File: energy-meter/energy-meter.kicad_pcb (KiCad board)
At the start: 2 copper layers, 82 x 62.5 mm, 87 parts, among them J1 Screw_Terminal_01x04, J27 Conn_01x04_Male, K1 G5RL-U1A-E, P1 PineNut, Q10 AP3400, Q11 AP3400, Q12 AP3400, Q14 AP3400, T1 AP-2500, T2 BV 202 0154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

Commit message: continue changing schematic
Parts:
- removed C69, C74: 47p, Capacitor_SMD:C_0603_1608Metric_Pad1.05x0.95mm_HandSolder
- removed C71, C73, C75, C76: 270p, Capacitor_SMD:C_0603_1608Metric_Pad1.05x0.95mm_HandSolder
- removed J27: Conn_01x04_Male, Connector_PinHeader_2.54mm:PinHeader_1x04_P2.54mm_Vertical
- removed R56, R57, R58, R60, R61, R62: 1k, Resistor_SMD:R_0603_1608Metric_Pad1.05x0.95mm_HandSolder
- removed R59, R63: 4k7, Resistor_SMD:R_0603_1608Metric_Pad1.05x0.95mm_HandSolder
- removed R65, R77, R83: 390k, Resistor_SMD:R_0603_1608Metric_Pad1.05x0.95mm_HandSolder
- removed R76, R78: 10R, 200 mW, Resistor_SMD:R_1206_3216Metric_Pad1.42x1.75mm_HandSolder
- added R1: 50R, 0.1%, Resistor_SMD:R_0603_1608Metric_Pad1.05x0.95mm_HandSolder, F.Cu at (127.9, 77.5)
- added R2: 50R, 0.1%, Resistor_SMD:R_0603_1608Metric_Pad1.05x0.95mm_HandSolder, F.Cu at (127.9, 80.0)
- added R3: 50R, 0.1%, Resistor_SMD:R_0603_1608Metric_Pad1.05x0.95mm_HandSolder, F.Cu at (132.2, 77.5)
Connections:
- net /Modified LCR Meter/IN0 renamed /Modified LCR Meter/VOLTAGE0
- net /Modified LCR Meter/IN1 renamed /Modified LCR Meter/VOLTAGE1
- net /Modified LCR Meter/OUT0_OFFSET renamed Net-(U10-Pad12)
- net /Modified LCR Meter/OUT1_OFFSET renamed Net-(U10-Pad15)
- net Net-(J1-Pad1) renamed PE
- D12 pad 1: /Modified LCR Meter/OUT0B -> /Modified LCR Meter/CURRENT1
- D12 pad 13: /Modified LCR Meter/OUT0B -> /Modified LCR Meter/CURRENT1
- D12 pad 14: /Modified LCR Meter/OUT0B -> /Modified LCR Meter/CURRENT1
- D12 pad 2: /Modified LCR Meter/OUT0B -> /Modified LCR Meter/CURRENT1
- D12 pad 6: /Modified LCR Meter/OUT1 -> /Modified LCR Meter/CURRENT0
- D12 pad 7: /Modified LCR Meter/OUT1 -> /Modified LCR Meter/CURRENT0
- D12 pad 8: /Modified LCR Meter/OUT1 -> /Modified LCR Meter/CURRENT0
- D12 pad 9: /Modified LCR Meter/OUT1 -> /Modified LCR Meter/CURRENT0
- J1 pad 2: Net-(J1-Pad2) -> N
- J1 pad 3: Net-(J1-Pad3) -> L_IN
- J1 pad 4: Net-(J1-Pad4) -> L_OUT
- K1 pad 3: Net-(K1-Pad3) -> L_OUT
- K1 pad 4: Net-(K1-Pad4) -> L_IN
- K1 pad 5: Net-(K1-Pad5) -> L_IN
- K1 pad 6: Net-(K1-Pad6) -> L_OUT
- R64 pad 2: /Modified LCR Meter/OUT0 -> /Modified LCR Meter/CURRENT0
- R66 pad 2: /Modified LCR Meter/CURR0 -> /Modified LCR Meter/CURRENT0
- R67 pad 2: /Modified LCR Meter/CURR1 -> /Modified LCR Meter/CURRENT1
- R84 pad 3: /Modified LCR Meter/CURR0 -> /Modified LCR Meter/CURRENT0
- R84 pad 4: /Modified LCR Meter/OUT0 -> /Modified LCR Meter/CURRENT0
- R85 pad 1: /Modified LCR Meter/OUT0 -> /Modified LCR Meter/CURRENT0
- R85 pad 2: /Modified LCR Meter/CURR0 -> /Modified LCR Meter/CURRENT0
- R86 pad 1: /Modified LCR Meter/OUT0 -> /Modified LCR Meter/CURRENT0
- R86 pad 2: /Modified LCR Meter/CURR0 -> /Modified LCR Meter/CURRENT0
- R95 pad 1: /Modified LCR Meter/OUT0 -> /Modified LCR Meter/CURRENT0
- R95 pad 2: /Modified LCR Meter/CURR0 -> /Modified LCR Meter/CURRENT0
- T2 pad 1: Net-(T2-Pad1) -> L_IN
- T2 pad 4: (no net) -> N
- U10 pad 18: /Modified LCR Meter/CURR1 -> /Modified LCR Meter/CURRENT1
- U11 pad 18: /Modified LCR Meter/CURR1 -> /Modified LCR Meter/CURRENT1
- U12 pad 18: /Modified LCR Meter/CURR1 -> /Modified LCR Meter/CURRENT1
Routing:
- net /Modified LCR Meter/CURRENT1: track 0.00 -> 39.5 mm, vias 0 -> 3
- net /Modified LCR Meter/CURR1: track 39.5 -> 0.00 mm, vias 3 -> 0
- net /Modified LCR Meter/CURRENT0: track 0.00 -> 32.4 mm
- net /Modified LCR Meter/CURR0: track 32.4 -> 0.00 mm
- net (no net): track 0.00 -> 27.8 mm, vias 0 -> 4
- net /LCR Meter/U10B-: track 25.9 -> 0.00 mm, vias 4 -> 0
- net GND: track 188.9 -> 164.5 mm, vias 18 -> 15
- net Net-(C73-Pad2): track 13.4 -> 0.00 mm, vias 2 -> 0
- net /LCR Meter/DAC0: track 11.2 -> 0.00 mm
- net /DAC0: track 0.00 -> 11.2 mm
- net Net-(C76-Pad2): track 10.7 -> 0.00 mm
- net Net-(C71-Pad1): track 10.2 -> 0.00 mm
- net Net-(C69-Pad1): track 6.86 -> 0.00 mm
- net Net-(C74-Pad1): track 5.68 -> 0.00 mm, vias 2 -> 0
- net Net-(R59-Pad2): track 5.43 -> 0.00 mm
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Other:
- board text added: "Energy Meter v1 c3pb, snowball"
- board text removed: "0"
- board text removed: "0b"
- board text removed: "1"
- board text removed: "1b"
- board text removed: "LCR Meter v1 c3pb, snowball"

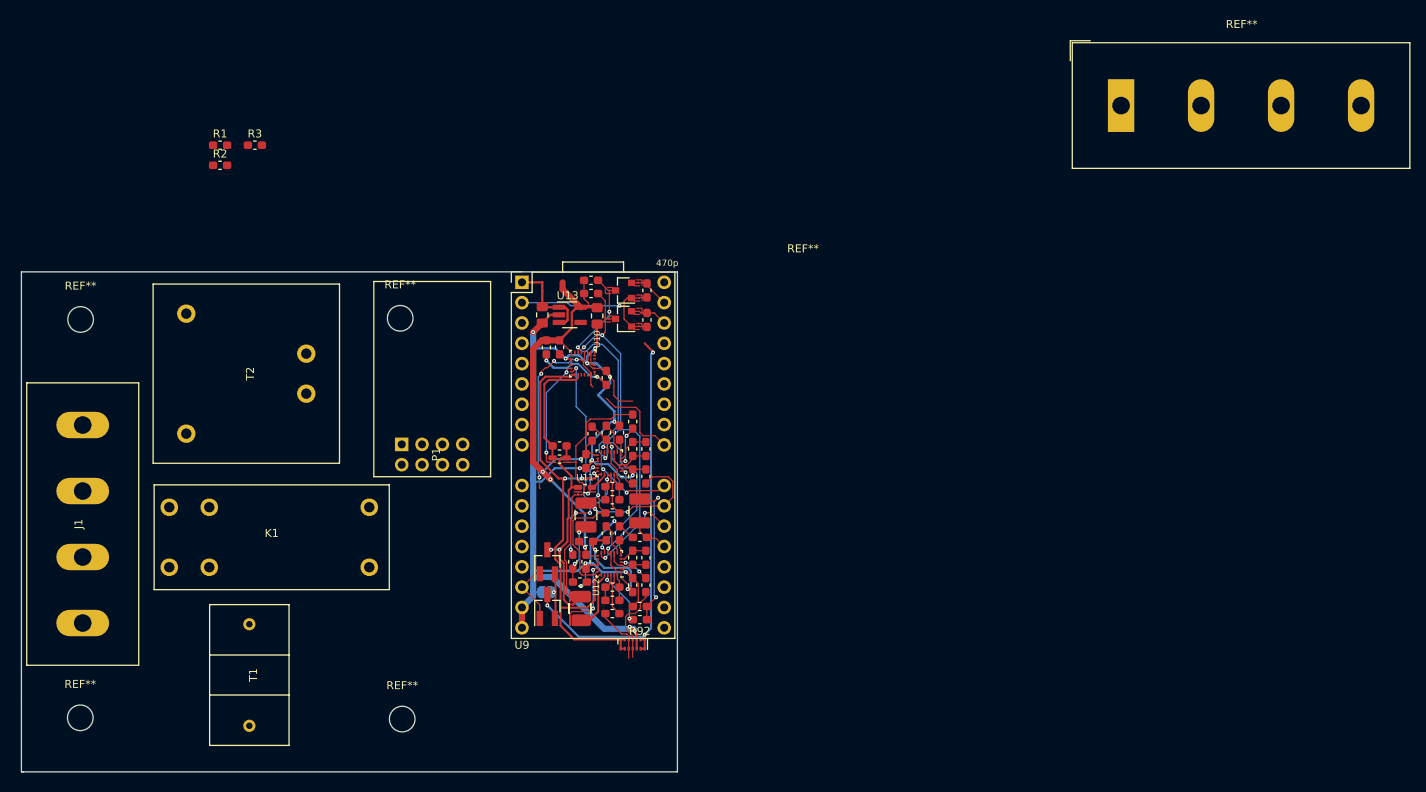
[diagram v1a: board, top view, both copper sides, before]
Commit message: remove two of the opamps
We can measure the voltage without an amplifier so let's do it. The other
was used for the LCR outputs, which we don't have here.
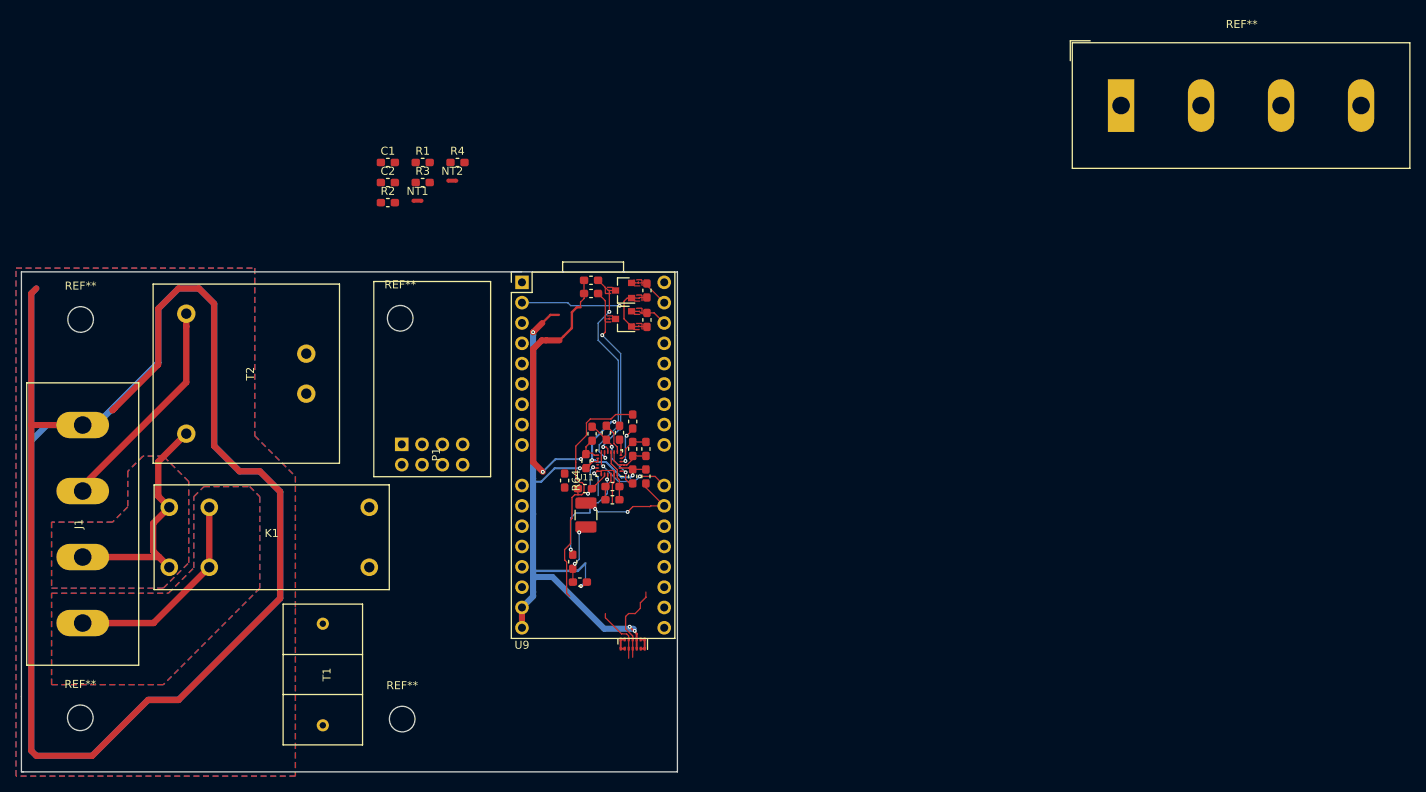
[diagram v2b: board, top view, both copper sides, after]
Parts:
- removed C65, C67, C70, C72: 100n, Capacitor_SMD:C_0603_1608Metric_Pad1.05x0.95mm_HandSolder
- removed C79, C80: 4.7p, Capacitor_SMD:C_0603_1608Metric_Pad1.05x0.95mm_HandSolder
- removed C81, C82: 1u, Capacitor_SMD:C_0805_2012Metric_Pad1.15x1.40mm_HandSolder
- removed C85: 270p, 1%, Capacitor_SMD:C_0603_1608Metric_Pad1.05x0.95mm_HandSolder
- removed FB1, FB3: 600R, 0.5A, Inductor_SMD:L_0603_1608Metric_Pad1.05x0.95mm_HandSolder
- removed JP20: SolderJumper_2_Open, Jumper:SolderJumper-2_P1.3mm_Open_RoundedPad1.0x1.5mm
- removed L5: 470u, Inductor_SMD:L_1210_3225Metric_Pad1.42x2.65mm_HandSolder
- removed Q12, Q14: AP3400, Package_TO_SOT_SMD:SOT-23_Handsoldering
- removed R67, R68, R69: 1k, Resistor_SMD:R_0603_1608Metric_Pad1.05x0.95mm_HandSolder
- removed R70, R71: 10k, Resistor_SMD:R_0603_1608Metric_Pad1.05x0.95mm_HandSolder
- removed R79, R80: 47k, Resistor_SMD:R_0603_1608Metric_Pad1.05x0.95mm_HandSolder
- removed R84: 20R, 100 mW, 0.1%, glowstone:R_0603_1608Metric_Pad1.05x0.95mm_HandSolder_Shunt
- removed R86: 2M, 0.1%, glowstone:R_1210_3225Metric_Pad1.42x2.65mm_HandSolder_Shunt
- removed R92, R93: 1k, 1%, Resistor_SMD:R_0603_1608Metric_Pad1.05x0.95mm_HandSolder
- removed R95: 1R, 0.1% (alternative to 2M), glowstone:R_1210_3225Metric_Pad1.42x2.65mm_HandSolder_Shunt
- removed U10, U12: SLG47004, glowstone:SLG47004
- removed U13: XC6227C381MR-G, Package_TO_SOT_SMD:SOT-23-5_HandSoldering
- added C1: 100n, Capacitor_SMD:C_0603_1608Metric_Pad1.05x0.95mm_HandSolder, F.Cu at (148.9, 79.7)
- added C2: 100n, Capacitor_SMD:C_0603_1608Metric_Pad1.05x0.95mm_HandSolder, F.Cu at (148.9, 82.2)
- added NT1: Net-Tie_2, NetTie:NetTie-2_SMD_Pad0.5mm, F.Cu at (152.6, 84.4)
- added NT2: Net-Tie_2, NetTie:NetTie-2_SMD_Pad0.5mm, F.Cu at (156.9, 81.9)
- added R4: 1k, 0.1%, Resistor_SMD:R_0603_1608Metric_Pad1.05x0.95mm_HandSolder, F.Cu at (157.6, 79.7)
- R1: value 50R, 0.1% -> 5k, 0.1%
- R2, R3: value 50R, 0.1% -> 1k, 0.1%
- R64: value 20R, 100 mW, 0.1% -> 50k, 0.1%
- R85: value 10k, 0.1% -> 50R, 0.1%; footprint glowstone:R_0603_1608Metric_Pad1.05x0.95mm_HandSolder_Shunt -> Resistor_SMD:R_0603_1608Metric_Pad1.05x0.95mm_HandSolder
- moved R1 25.4 mm to (153.2, 79.7)
- moved R2 21.5 mm to (148.9, 84.7)
- moved R3 21.5 mm to (153.2, 82.2)
- moved T1 9.19 mm to (140.7, 143.7)
- moved R64 4.38 mm to (171.0, 119.4), turned to 270 degrees
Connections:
- C68 pad 1: VDDA -> +3V3
- D12 pad 1: /Modified LCR Meter/CURRENT1 -> /CURRENT1
- D12 pad 11: /Modified LCR Meter/VOLTAGE1 -> /VOLTAGE1
- D12 pad 12: /Modified LCR Meter/VOLTAGE0 -> /VOLTAGE0
- D12 pad 13: /Modified LCR Meter/CURRENT1 -> /CURRENT1
- D12 pad 14: /Modified LCR Meter/CURRENT1 -> /CURRENT1
- D12 pad 2: /Modified LCR Meter/CURRENT1 -> /CURRENT1
- D12 pad 3: /Modified LCR Meter/VOLTAGE0 -> /VOLTAGE0
- D12 pad 4: /Modified LCR Meter/VOLTAGE1 -> /VOLTAGE1
- D12 pad 6: /Modified LCR Meter/CURRENT0 -> /CURRENT0
- D12 pad 7: /Modified LCR Meter/CURRENT0 -> /CURRENT0
- D12 pad 8: /Modified LCR Meter/CURRENT0 -> /CURRENT0
- D12 pad 9: /Modified LCR Meter/CURRENT0 -> /CURRENT0
- FB2 pad 2: VDDA -> +3V3
- R1 pad 1: Net-(R1-Pad1) -> /VOLTAGE0
- R2 pad 1: Net-(R2-Pad1) -> /VOLTAGE1
- R2 pad 2: Net-(R2-Pad2) -> /VOLTAGE0
- R3 pad 1: Net-(R3-Pad1) -> +3V3
- R3 pad 2: Net-(R1-Pad1) -> /BIAS
- R54 pad 1: VDDA -> +3V3
- R55 pad 1: VDDA -> +3V3
- R64 pad 1: /Modified LCR Meter/AS0A_1 -> /Modified LCR Meter/AS1A_2
- R64 pad 2: /Modified LCR Meter/CURRENT0 -> /CURRENT0
- R66 pad 2: /Modified LCR Meter/CURRENT0 -> /CURRENT0
- R85 pad 1: /Modified LCR Meter/CURRENT0 -> /CURRENT0
- R85 pad 2: /Modified LCR Meter/CURRENT0 -> /Modified LCR Meter/AS0A_2
- T1 pad 1: Net-(R2-Pad1) -> /CURRENT1
- T1 pad 2: Net-(R2-Pad2) -> /CURRENT0
- T2 pad 6: Net-(R3-Pad1) -> /VOLTAGE1
- U11 pad 13: VDDA -> +3V3
- U11 pad 18: /Modified LCR Meter/CURRENT1 -> /CURRENT1
- U11 pad 19: /Modified LCR Meter/OUT0B -> /CURRENT1
- U11 pad 23: Net-(R67-Pad1) -> /CURRENT1
- U9 pad 32: Net-(U9-Pad32) -> /VOLTAGE0
- U9 pad 33: Net-(U9-Pad33) -> /VOLTAGE1
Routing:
- net PE: track 0.00 -> 344.9 mm
- net GND: track 164.5 -> 98.6 mm, vias 15 -> 8
- net VDDA: track 63.5 -> 0.00 mm, vias 4 -> 0
- net /Modified LCR Meter/OUT0B: track 61.2 -> 0.00 mm, vias 2 -> 0
- net /Modified LCR Meter/OUT1: track 55.3 -> 0.00 mm, vias 3 -> 0
- net /Modified LCR Meter/CURRENT1: track 39.5 -> 0.00 mm, vias 3 -> 0
- net +3V3: track 21.3 -> 59.9 mm, vias 1 -> 3
- net /CURRENT0: track 0.00 -> 33.4 mm
- net /Modified LCR Meter/CURRENT0: track 32.4 -> 0.00 mm
- net L_IN: track 0.00 -> 31.7 mm
- net (no net): track 27.8 -> 0.00 mm, vias 4 -> 0
- net N: track 0.00 -> 27.5 mm
- net /Modified LCR Meter/OUT0: track 26.7 -> 0.00 mm, vias 2 -> 0
- net L_OUT: track 0.00 -> 26.2 mm
- net /Modified LCR Meter/SDA_5V: track 52.7 -> 27.3 mm, vias 4 -> 2
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- added copper zone on B.Cu, net L_IN
- added copper zone on F.Cu, net L_IN
- added copper zone on B.Cu, net L_OUT
- added copper zone on F.Cu, net L_OUT
- added copper zone on B.Cu, net PE
- added copper zone on F.Cu, net PE
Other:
- board text removed: "470p"

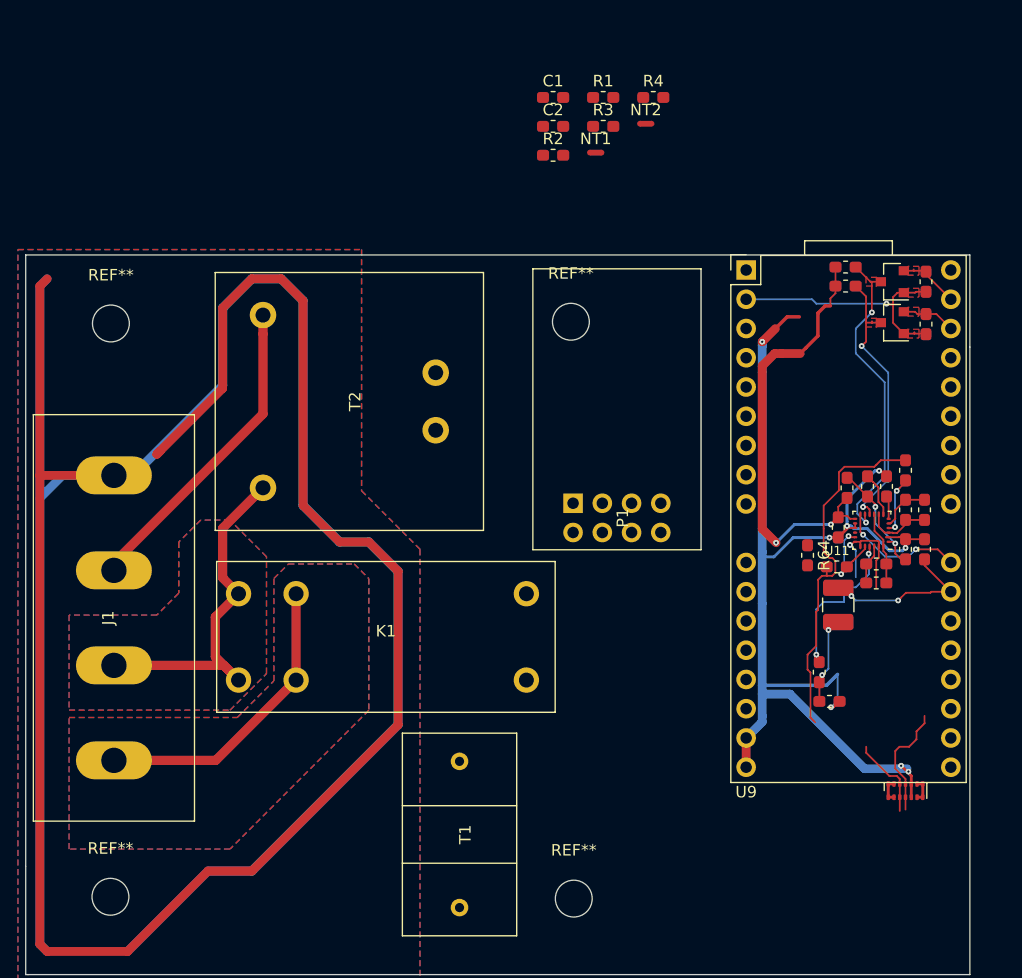
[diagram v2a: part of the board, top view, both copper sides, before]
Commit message: everything done except current measurement
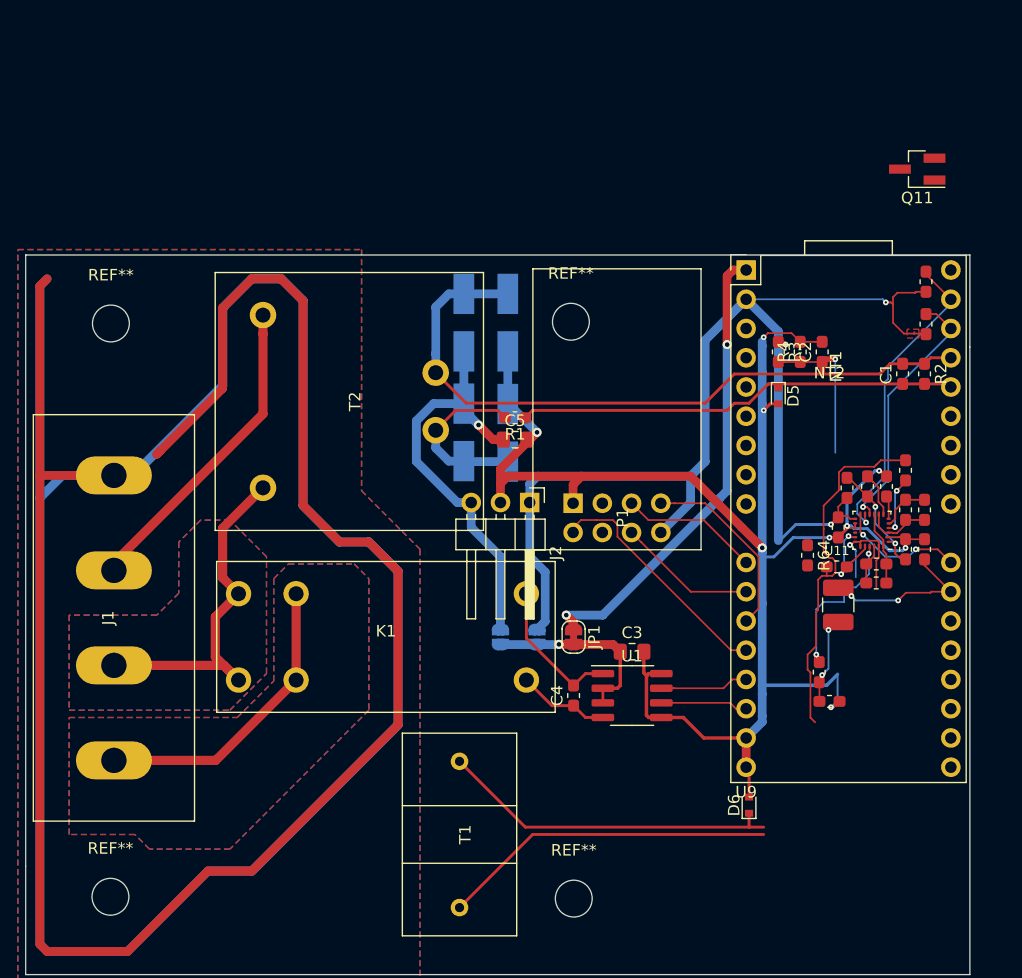
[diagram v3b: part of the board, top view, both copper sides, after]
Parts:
- removed D12: SP3012-06UTG, glowstone:UDFN-14_3.5x1.35mm_P0.5mm
- removed Q10: AP3400, Package_TO_SOT_SMD:SOT-23
- removed R54, R55: 10k, Resistor_SMD:R_0603_1608Metric_Pad1.05x0.95mm_HandSolder
- added C3: 10u, Capacitor_SMD:C_0805_2012Metric_Pad1.15x1.40mm_HandSolder, F.Cu at (155.7, 127.8)
- added C4: 100n, Capacitor_SMD:C_0603_1608Metric_Pad1.05x0.95mm_HandSolder, F.Cu at (150.7, 131.6)
- added C5: 10u, Capacitor_SMD:C_0805_2012Metric_Pad1.15x1.40mm_HandSolder, F.Cu at (145.6, 109.4)
- added D1: D_Schottky, Diode_SMD:D_SMA_Handsoldering, B.Cu at (141.1, 108.7)
- added D2: D_Schottky, Diode_SMD:D_SMA_Handsoldering, B.Cu at (144.9, 108.8)
- added D3: D_Schottky, Diode_SMD:D_SMA_Handsoldering, B.Cu at (141.1, 99.2)
- added D4: D_Schottky, Diode_SMD:D_SMA_Handsoldering, B.Cu at (144.9, 99.2)
- added D5: ESD5Z5.0T1G, Diode_SMD:D_SOD-523, F.Cu at (168.4, 105.6)
- added D6: ESD5Z5.0T1G, Diode_SMD:D_SOD-523, F.Cu at (165.9, 141.1)
- added J2: Conn_01x03, Connector_PinHeader_2.54mm:PinHeader_1x03_P2.54mm_Horizontal, F.Cu at (146.8, 114.8)
- added JP1: SolderJumper_2_Bridged, Jumper:SolderJumper-2_P1.3mm_Bridged_RoundedPad1.0x1.5mm, F.Cu at (150.7, 126.5)
- added JP2: SolderJumper_2_Open, Jumper:SolderJumper-2_P1.3mm_Open_RoundedPad1.0x1.5mm, B.Cu at (147.5, 126.5)
- added JP3: SolderJumper_2_Open, Jumper:SolderJumper-2_P1.3mm_Open_RoundedPad1.0x1.5mm, B.Cu at (144.3, 126.5)
- added U1: L9110S, Package_SO:SOP-8_3.76x4.96mm_P1.27mm, F.Cu at (155.7, 131.6)
- C1: value 100n -> 10n
- Q11: footprint Package_TO_SOT_SMD:SOT-23 -> Package_TO_SOT_SMD:SOT-23_Handsoldering
- moved C1 38.7 mm to (179.2, 103.7), turned to 90 degrees
- moved R2 37.4 mm to (181.1, 103.7), turned to 270 degrees
- moved C2 30.5 mm to (172.2, 101.8), turned to 90 degrees
- moved R1 28.8 mm to (145.6, 107.5), turned to 180 degrees
- moved NT1 27.1 mm to (172.2, 103.0), turned to 270 degrees
- moved NT2 25.9 mm to (172.9, 102.4), turned to 180 degrees
- moved R4 25.5 mm to (170.3, 101.8), turned to 90 degrees
- moved R3 24.8 mm to (168.4, 101.8), turned to 270 degrees
- moved Q11 10.0 mm to (180.5, 85.9)
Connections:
- net /OP2_OUT_F renamed Net-(U9-Pad23)
- net /OUT1_to_MCU renamed Net-(U9-Pad30)
- net /TEMP2 renamed Net-(U9-Pad24)
- net Net-(R1-Pad2) renamed /6VAC
- C68 pad 1: +3V3 -> VDDA
- P1 pad 5: Net-(P1-Pad5) -> /PINENUT_IO8_BOOT
- P1 pad 6: Net-(P1-Pad6) -> /PINENUT_RST
- Q11 pad 1: +3V3 -> Net-(Q11-Pad1)
- Q11 pad 2: /SDA -> Net-(Q11-Pad2)
- Q11 pad 3: /Modified LCR Meter/SDA_5V -> Net-(Q11-Pad3)
- U11 pad 10: /Modified LCR Meter/SCL_5V -> /SCL
- U11 pad 11: /Modified LCR Meter/SDA_5V -> /SDA
- U9 pad 1: /5V -> +5V
- U9 pad 11: Net-(U9-Pad11) -> /PINENUT_IO8_BOOT
- U9 pad 12: Net-(U9-Pad12) -> /PINENUT_RST
- U9 pad 13: /U10B_10k -> /PINENUT_RX
- U9 pad 14: Net-(U9-Pad14) -> /PINENUT_TX
- U9 pad 15: Net-(U9-Pad15) -> /RELAY_SET
- U9 pad 16: /OUT01_SHORT -> /RELAY_RESET
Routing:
- net /VOLTAGE1: track 10.0 -> 60.7 mm
- net GND: track 98.6 -> 147.2 mm, vias 8 -> 9
- net +3V3: track 59.9 -> 106.8 mm
- net +5V: track 0.00 -> 40.5 mm, vias 0 -> 2
- net +6V: track 0.00 -> 36.2 mm, vias 0 -> 1
- net /CURRENT1: track 12.3 -> 47.3 mm, vias 1 -> 2
- net /VOLTAGE0: track 7.16 -> 38.7 mm
- net /CURRENT0: track 33.4 -> 61.2 mm
- net /Modified LCR Meter/SDA_5V: track 27.3 -> 0.00 mm, vias 2 -> 0
- net /Modified LCR Meter/SCL_5V: track 24.2 -> 0.00 mm, vias 2 -> 0
- net /SDA: track 4.99 -> 27.1 mm, vias 0 -> 1
- net /PINENUT_TX: track 0.00 -> 21.0 mm
- net /SCL: track 4.68 -> 22.5 mm, vias 0 -> 1
- net Net-(C3-Pad1): track 0.00 -> 16.5 mm, vias 0 -> 1
- net /PINENUT_RX: track 0.00 -> 16.4 mm
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- removed copper zone on F.Cu, net /LCR Meter/SCL
- removed copper zone on F.Cu, net /LCR Meter/SCL_5V
- removed copper zone on F.Cu, net /LCR Meter/SDA
- removed copper zone on F.Cu, net /LCR Meter/SDA_5V
